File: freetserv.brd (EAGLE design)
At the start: 91.4 x 82.5 mm, 62 parts, among them IC2 SN75240PW, Q1 12MHz, Q2 6MHz, U1 MCP16311-E/MS

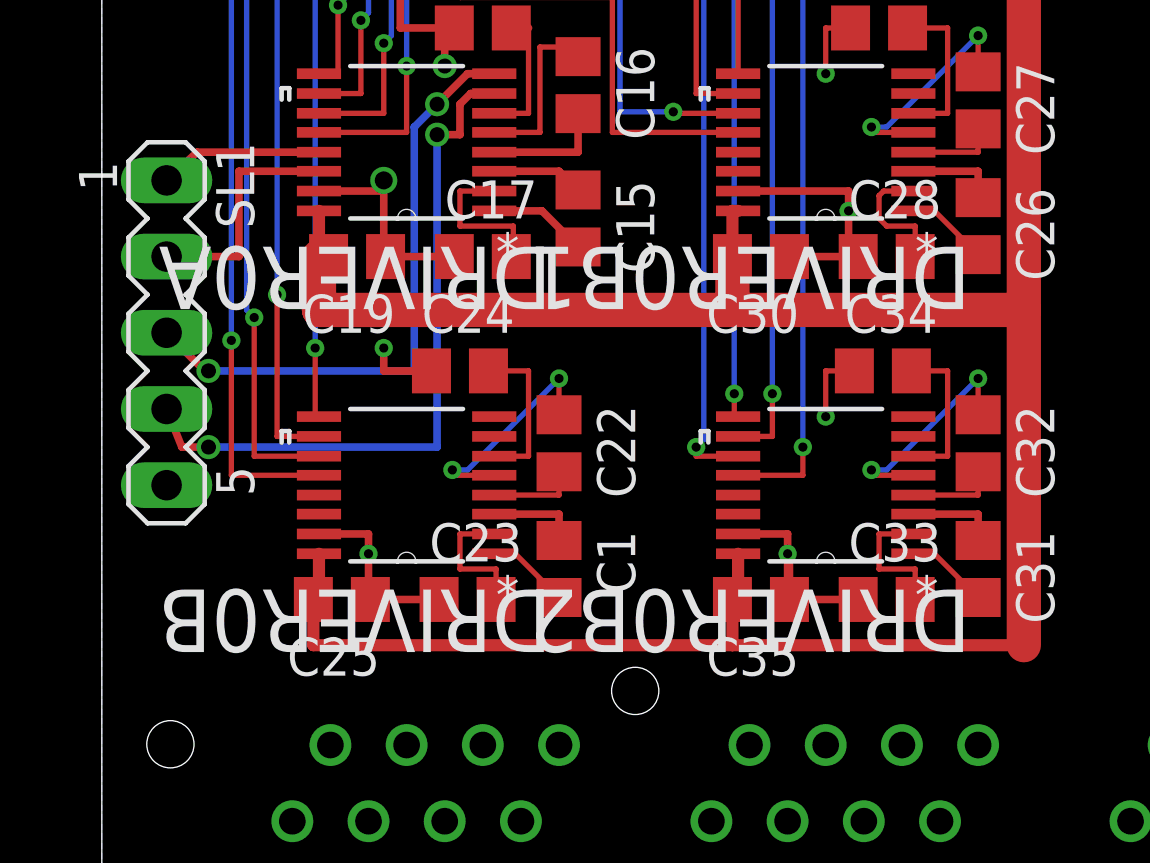
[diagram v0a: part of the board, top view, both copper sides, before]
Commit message: add circle to pin 1 for the MAX3232
Also use the correct IC (E variant for ESD protection) and rename the
ICs properly (DRIVER → DRV so that the name fits, suffix 0A-0D like the
FTDI outputs).

see issue #2
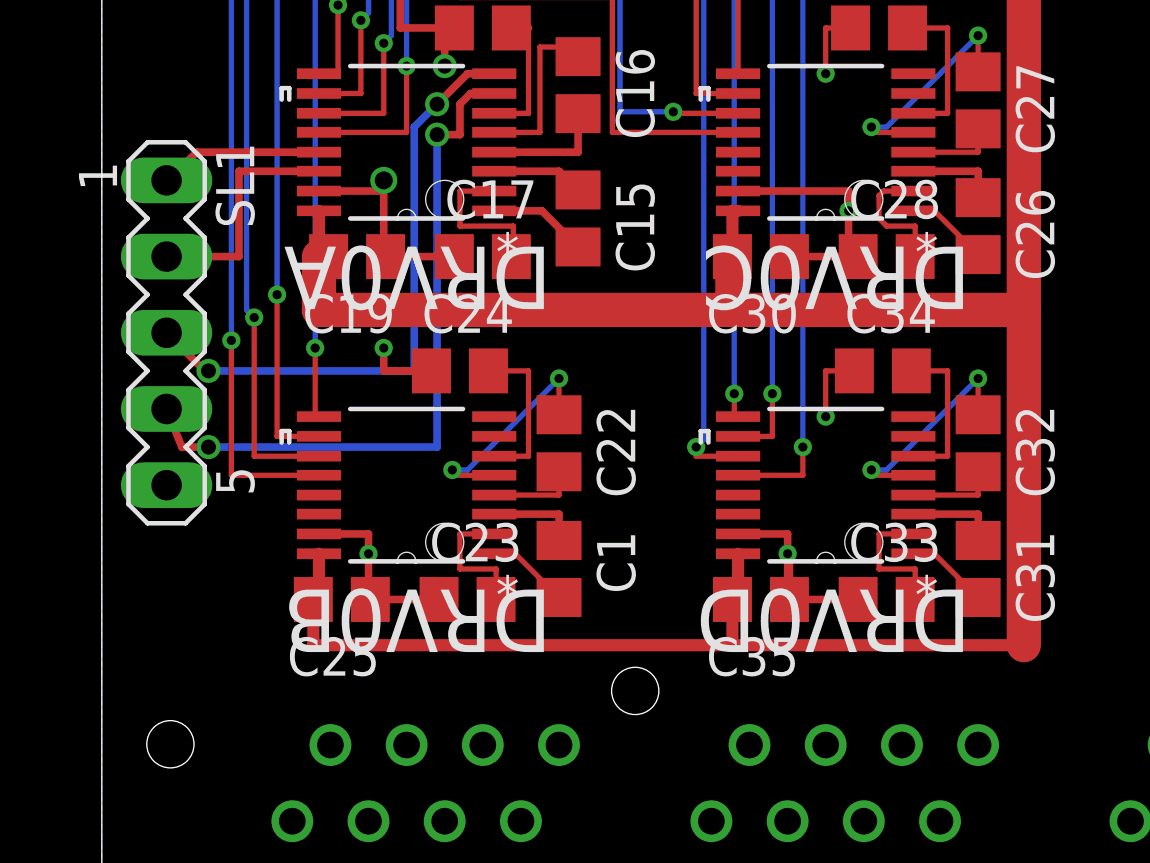
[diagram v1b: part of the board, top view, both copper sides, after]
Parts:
- DRV0A, DRV0B, DRV0C, DRV0D: value MAX3232CPWR -> MAX3232ECPW
- renumbered DRIVER0A to DRV0A, DRIVER0B to DRV0B, DRIVER0B1 to DRV0C, DRIVER0B2 to DRV0D

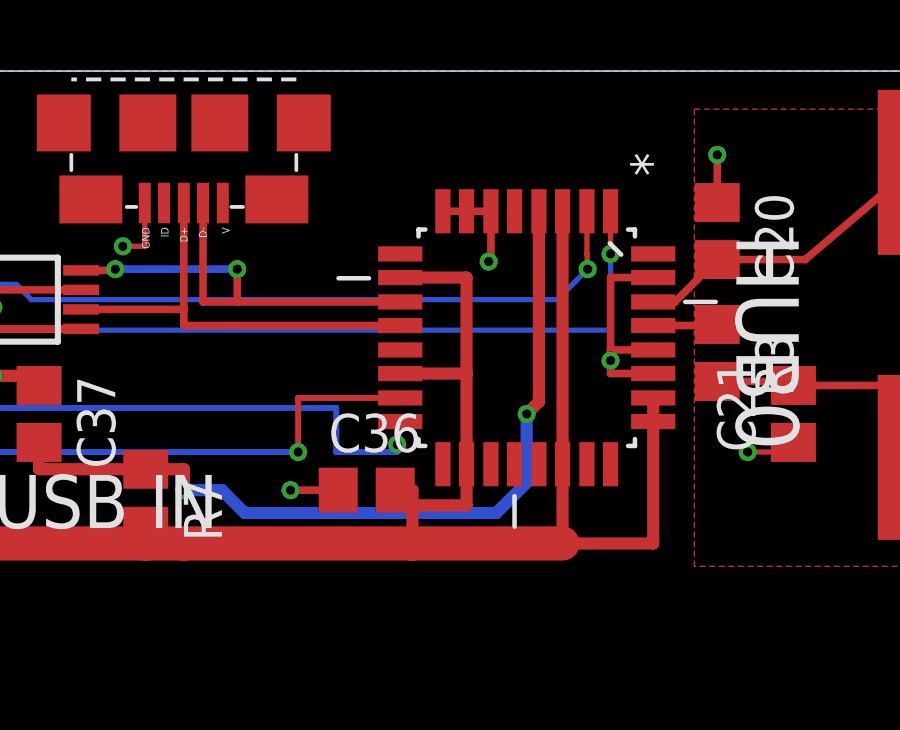
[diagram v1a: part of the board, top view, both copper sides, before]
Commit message: add circle to pin 1 of the TUSB2046, increase pad size while at it
fixes #2
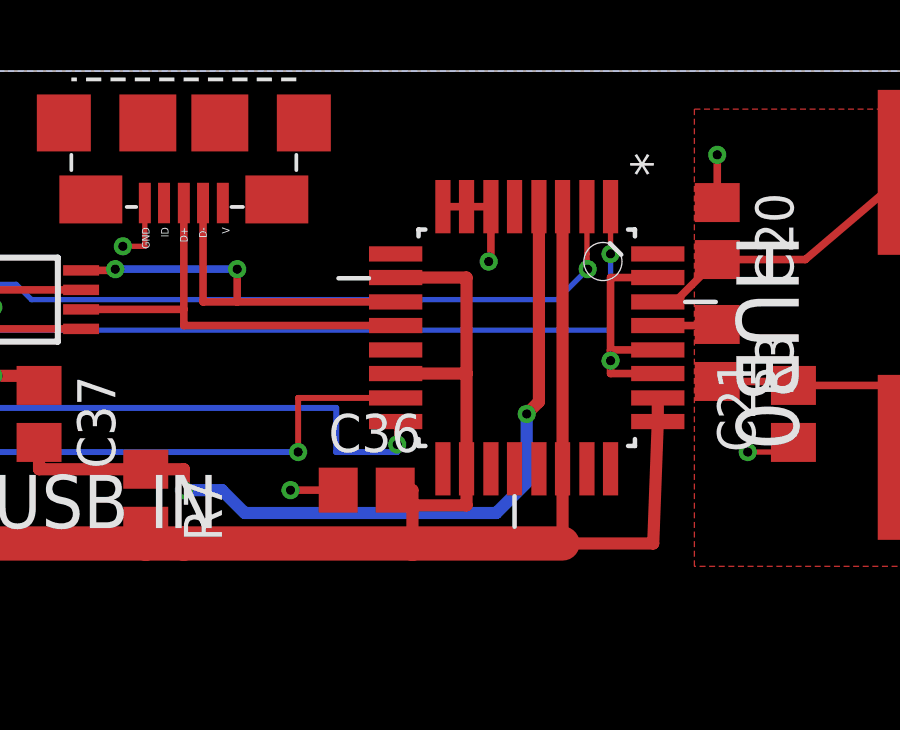
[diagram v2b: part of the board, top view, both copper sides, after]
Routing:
- net GND: track 137.1 -> 137.8 mm
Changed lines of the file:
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@@
 <via x="73.66" y="76.2" extent="1-16" drill="0.3048"/>
 <wire x1="73.66" y1="76.2" x2="73.7362" y2="76.2" width="0.254" layer="1"/>
-<wire x1="73.7362" y1="76.2" x2="73.7362" y2="77.8764" width="0.254" layer="1"/>
-<wire x1="73.7362" y1="77.8764" x2="72.9234" y2="77.8764" width="0.254" layer="1"/>
-<wire x1="72.9234" y1="77.8764" x2="72.136" y2="77.8764" width="0.254" layer="1"/>
-<wire x1="72.136" y1="77.8764" x2="72.2122" y2="77.8764" width="0.254" layer="1"/>
+<wire x1="73.7362" y1="76.2" x2="73.7362" y2="78.0288" width="0.254" layer="1"/>
+<wire x1="73.7362" y1="78.0288" x2="72.9234" y2="78.0288" width="0.254" layer="1"/>
+<wire x1="72.9234" y1="78.0288" x2="72.136" y2="78.0288" width="0.254" layer="1"/>
+<wire x1="72.136" y1="78.0288" x2="72.2122" y2="77.8764" width="0.254" layer="1"/>
 <via x="77.724" y="72.898" extent="1-16" drill="0.3048"/>
-<wire x1="79.1464" y1="72.4662" x2="77.724" y2="72.4662" width="0.254" layer="1"/>
+<wire x1="79.2988" y1="72.4662" x2="77.724" y2="72.4662" width="0.254" layer="1"/>
 <wire x1="77.724" y1="72.4662" x2="77.724" y2="72.898" width="0.254" layer="1"/>
-<wire x1="79.1464" y1="73.2536" x2="77.724" y2="73.2536" width="0.254" layer="1"/>
+<wire x1="79.2988" y1="73.2536" x2="77.724" y2="73.2536" width="0.254" layer="1"/>
 <wire x1="77.724" y1="73.2536" x2="77.724" y2="72.898" width="0.254" layer="1"/>
-<wire x1="79.1464" y1="75.6666" x2="77.724" y2="75.6666" width="0.254" layer="1"/>
+<wire x1="79.2988" y1="75.6666" x2="77.724" y2="75.6666" width="0.254" layer="1"/>
 <wire x1="77.724" y1="75.6666" x2="77.724" y2="72.898" width="0.254" layer="1"/>
 <via x="81.28" y="79.756" extent="1-16" drill="0.3048"/>
@@
 <wire x1="77.724" y1="73.914" x2="77.724" y2="76.454" width="0.1778" layer="16"/>
 <via x="77.724" y="76.454" extent="1-16" drill="0.3048"/>
-<wire x1="77.724" y1="76.454" x2="77.724" y2="77.8764" width="0.1778" layer="1"/>
+<wire x1="77.724" y1="76.454" x2="77.724" y2="78.0288" width="0.1778" layer="1"/>
 <contactref element="R6" pad="1"/>
 <wire x1="55.88" y1="73.914" x2="55.88" y2="71.12" width="0.254" layer="1"/>
@@
 <via x="76.962" y="75.946" extent="1-16" drill="0.3048"/>
 <wire x1="76.962" y1="75.946" x2="76.9366" y2="76.454" width="0.1778" layer="1"/>
-<wire x1="76.9366" y1="76.454" x2="76.9366" y2="77.8764" width="0.1778" layer="1"/>
+<wire x1="76.9366" y1="76.454" x2="76.9366" y2="78.0288" width="0.1778" layer="1"/>
 <wire x1="76.962" y1="75.946" x2="75.946" y2="74.93" width="0.1778" layer="16"/>
 <wire x1="75.946" y1="74.93" x2="58.42" y2="74.93" width="0.1778" layer="16"/>
@@
 <via x="67.31" y="69.85" extent="1-16" drill="0.3048"/>
 <wire x1="67.31" y1="69.85" x2="67.31" y2="71.6534" width="0.2" layer="1"/>
-<wire x1="67.31" y1="71.6534" x2="70.7136" y2="71.6534" width="0.2" layer="1"/>
+<wire x1="67.31" y1="71.6534" x2="70.5612" y2="71.6534" width="0.2" layer="1"/>
 </signal>
 <signal name="USB0_D2_P" class="1">
@@
 <via x="70.612" y="70.104" extent="1-16" drill="0.3048"/>
 <wire x1="70.612" y1="70.104" x2="70.612" y2="70.866" width="0.2" layer="1"/>
-<wire x1="70.612" y1="70.866" x2="70.7136" y2="70.866" width="0.2" layer="1"/>
+<wire x1="70.612" y1="70.866" x2="70.5612" y2="70.866" width="0.2" layer="1"/>
 <wire x1="68.58" y1="71.32" x2="68.58" y2="69.85" width="0.2" layer="16"/>
 <wire x1="68.58" y1="69.85" x2="70.612" y2="69.85" width="0.2" layer="16"/>
@@
 <via x="74.93" y="71.12" extent="1-16" drill="0.3048"/>
 <wire x1="74.93" y1="71.12" x2="75.3364" y2="71.5264" width="0.4064" layer="1"/>
-<wire x1="75.3364" y1="71.5264" x2="75.3364" y2="77.8764" width="0.4064" layer="1"/>
+<wire x1="75.3364" y1="71.5264" x2="75.3364" y2="78.0288" width="0.4064" layer="1"/>
 <wire x1="9.95" y1="60.464" x2="58.674" y2="69.276" width="0" layer="19" extent="1-1"/>
 </signal>
@@
 <contactref element="Q2" pad="1"/>
 <contactref element="HUB0" pad="30"/>
-<wire x1="79.1464" y1="74.8538" x2="79.8678" y2="74.8538" width="0.254" layer="1"/>
+<wire x1="79.2988" y1="74.8538" x2="79.8678" y2="74.8538" width="0.254" layer="1"/>
 <wire x1="79.8678" y1="74.8538" x2="81.28" y2="76.266" width="0.254" layer="1"/>
 <wire x1="81.28" y1="76.266" x2="84.216" y2="76.266" width="0.254" layer="1"/>
@@
 <contactref element="R3" pad="1"/>
 <contactref element="HUB0" pad="29"/>
-<wire x1="79.1464" y1="74.0664" x2="81.2444" y2="74.0664" width="0.254" layer="1"/>
+<wire x1="79.2988" y1="74.0664" x2="81.2444" y2="74.0664" width="0.254" layer="1"/>
 <wire x1="81.2444" y1="74.0664" x2="81.28" y2="74.102" width="0.254" layer="1"/>
 </signal>
@@
 <wire x1="63.5" y1="66.802" x2="62.23" y2="66.802" width="1.143" layer="1"/>
 <wire x1="62.23" y1="66.802" x2="40.64" y2="66.802" width="1.143" layer="1"/>
-<wire x1="76.1238" y1="69.4436" x2="76.1238" y2="66.802" width="0.4064" layer="1"/>
-<wire x1="79.1464" y1="70.866" x2="79.1464" y2="66.802" width="0.4064" layer="1"/>
+<wire x1="76.1238" y1="69.2912" x2="76.1238" y2="66.802" width="0.4064" layer="1"/>
+<wire x1="79.2988" y1="70.866" x2="79.1464" y2="66.802" width="0.4064" layer="1"/>
 <wire x1="79.1464" y1="66.802" x2="76.1238" y2="66.802" width="0.4064" layer="1"/>
-<wire x1="79.1464" y1="70.866" x2="79.1464" y2="71.6534" width="0.4064" layer="1"/>
-<wire x1="70.7136" y1="72.4662" x2="72.9234" y2="72.4662" width="0.4064" layer="1"/>
-<wire x1="72.9234" y1="72.4662" x2="72.9234" y2="69.4436" width="0.4064" layer="1"/>
-<wire x1="70.7136" y1="75.6666" x2="72.9234" y2="75.6666" width="0.4064" layer="1"/>
+<wire x1="79.2988" y1="70.866" x2="79.2988" y2="71.6534" width="0.4064" layer="1"/>
+<wire x1="70.5612" y1="72.4662" x2="72.9234" y2="72.4662" width="0.4064" layer="1"/>
+<wire x1="72.9234" y1="72.4662" x2="72.9234" y2="69.2912" width="0.4064" layer="1"/>
+<wire x1="70.5612" y1="75.6666" x2="72.9234" y2="75.6666" width="0.4064" layer="1"/>
 <wire x1="72.9234" y1="75.6666" x2="72.9234" y2="72.4662" width="0.4064" layer="1"/>
-<wire x1="76.1238" y1="77.8764" x2="76.1238" y2="69.4436" width="0.4064" layer="1"/>
+<wire x1="76.1238" y1="78.0288" x2="76.1238" y2="69.2912" width="0.4064" layer="1"/>
 <contactref element="C36" pad="2"/>
 <wire x1="70.546" y1="68.58" x2="71.12" y2="68.58" width="0.4064" layer="1"/>
 <wire x1="71.12" y1="68.58" x2="71.12" y2="66.802" width="0.4064" layer="1"/>
-<wire x1="72.9234" y1="69.4436" x2="72.9234" y2="68.072" width="0.4064" layer="1"/>
+<wire x1="72.9234" y1="69.2912" x2="72.9234" y2="68.072" width="0.4064" layer="1"/>
 <wire x1="72.9234" y1="68.072" x2="70.612" y2="68.072" width="0.4064" layer="1"/>
 <wire x1="70.612" y1="68.072" x2="70.612" y2="68.58" width="0.4064" layer="1"/>
@@
 <contactref element="HUB0" pad="12"/>
 <contactref element="USB_IN" pad="D+"/>
-<wire x1="70.7136" y1="74.0664" x2="63.5" y2="74.0664" width="0.254" layer="1"/>
+<wire x1="70.5612" y1="74.0664" x2="63.5" y2="74.0664" width="0.254" layer="1"/>
 <wire x1="63.5" y1="74.605" x2="63.5" y2="78.15" width="0.254" layer="1"/>
 <contactref element="IC2" pad="6"/>
@@
 <contactref element="HUB0" pad="11"/>
 <contactref element="USB_IN" pad="D-"/>
-<wire x1="70.7136" y1="74.8538" x2="65.278" y2="74.8538" width="0.254" layer="1"/>
+<wire x1="70.5612" y1="74.8538" x2="65.278" y2="74.8538" width="0.254" layer="1"/>
 <wire x1="65.278" y1="74.8538" x2="64.14" y2="74.8538" width="0.254" layer="1"/>
 <wire x1="64.14" y1="74.8538" x2="64.14" y2="78.15" width="0.254" layer="1"/>

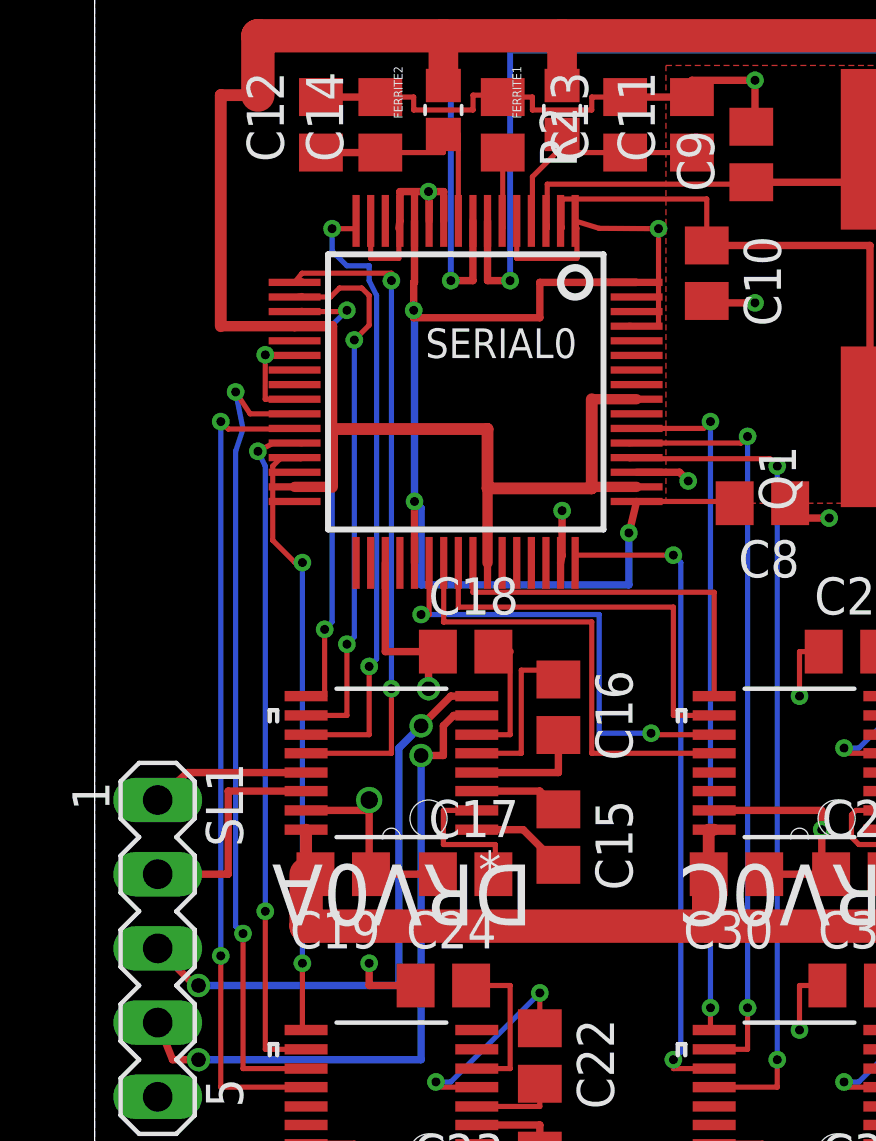
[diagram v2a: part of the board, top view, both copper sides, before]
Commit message: add capacitors for VCORE/VIO
fixes #12
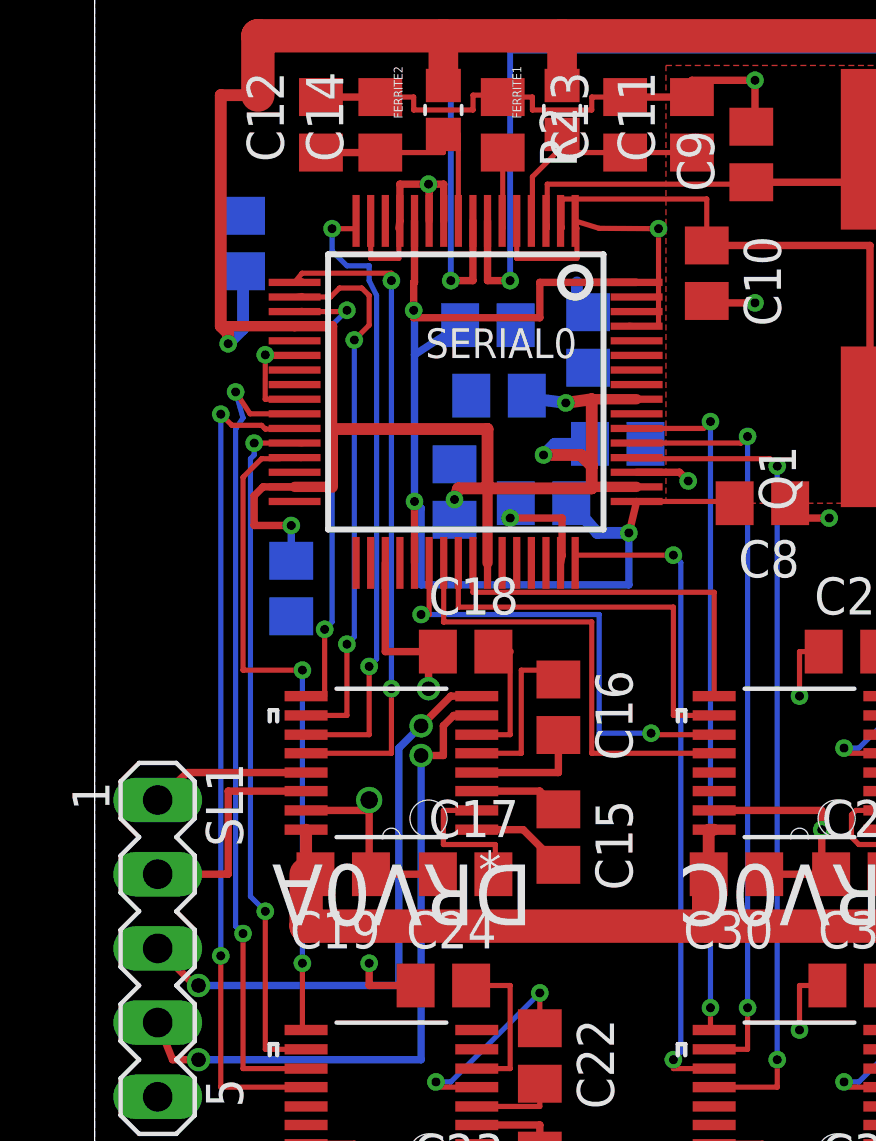
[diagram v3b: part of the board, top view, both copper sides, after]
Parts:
- added C38, C39, C40, C41, C42, C43, C44, C45: 0.1uF, resistor:C0805
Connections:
- removed net N$12: C8.2, SERIAL0.12, SERIAL0.37, SERIAL0.49, SERIAL0.64
- new net +1V8: C38.1, C39.1, C40.1, C8.2, SERIAL0.12, SERIAL0.37, SERIAL0.49, SERIAL0.64
- net +3V3: now also C41.1, C42.1, C43.1, C44.1, C45.1
- net GND: now also C38.2, C39.2, C40.2, C41.2, C42.2, C43.2, C44.2, C45.2
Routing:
- net +1V8: track 0.00 -> 44.2 mm, vias 0 -> 3
- net N$12: track 38.7 -> 0.00 mm, vias 3 -> 0
- net +3V3: track 290.4 -> 306.8 mm, vias 0 -> 5
- net GND: track 137.8 -> 140.1 mm
- net N$48: track 21.3 -> 22.8 mm
- net N$47: track 23.5 -> 24.1 mm
